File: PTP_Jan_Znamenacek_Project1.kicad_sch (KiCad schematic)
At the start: 0 parts

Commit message: Ispunjena sastavnica
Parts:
- added R1, R2: R_Small, symbol Device:R_Small
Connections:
- new net +3V3: R1.1
- new net GND: R2.2
- new net U_iz: R1.2, R2.1
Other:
- company: (none) -> TVZ
- title: (none) -> BCD Brojač

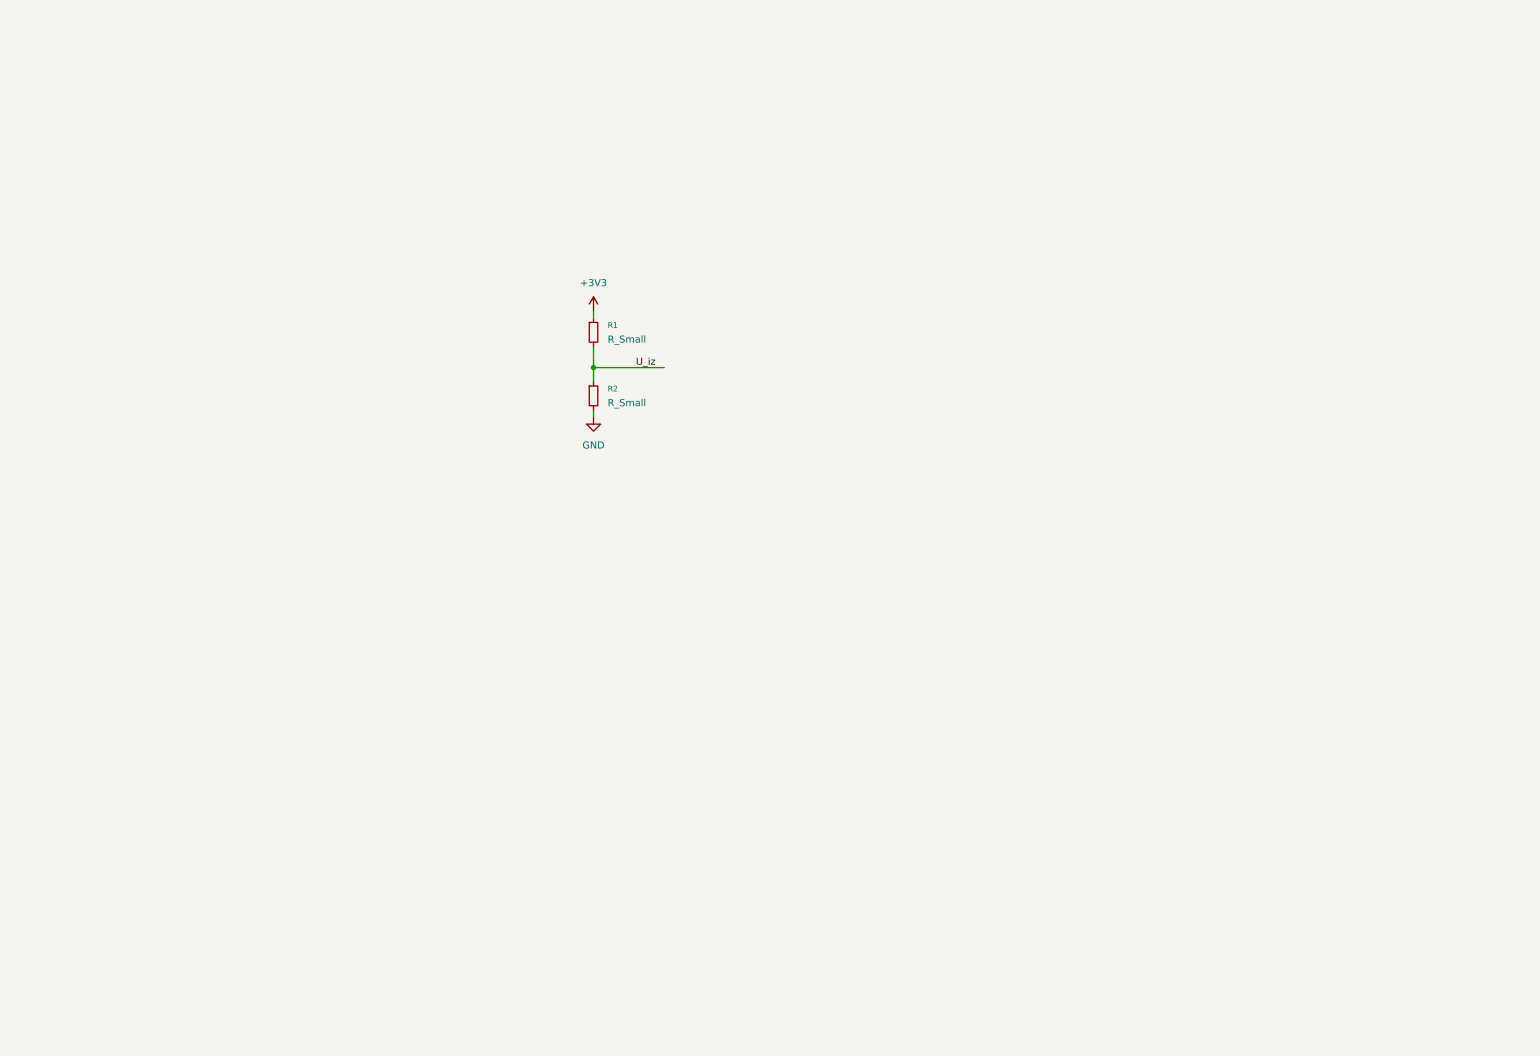
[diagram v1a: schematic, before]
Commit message: Dodan NE555P
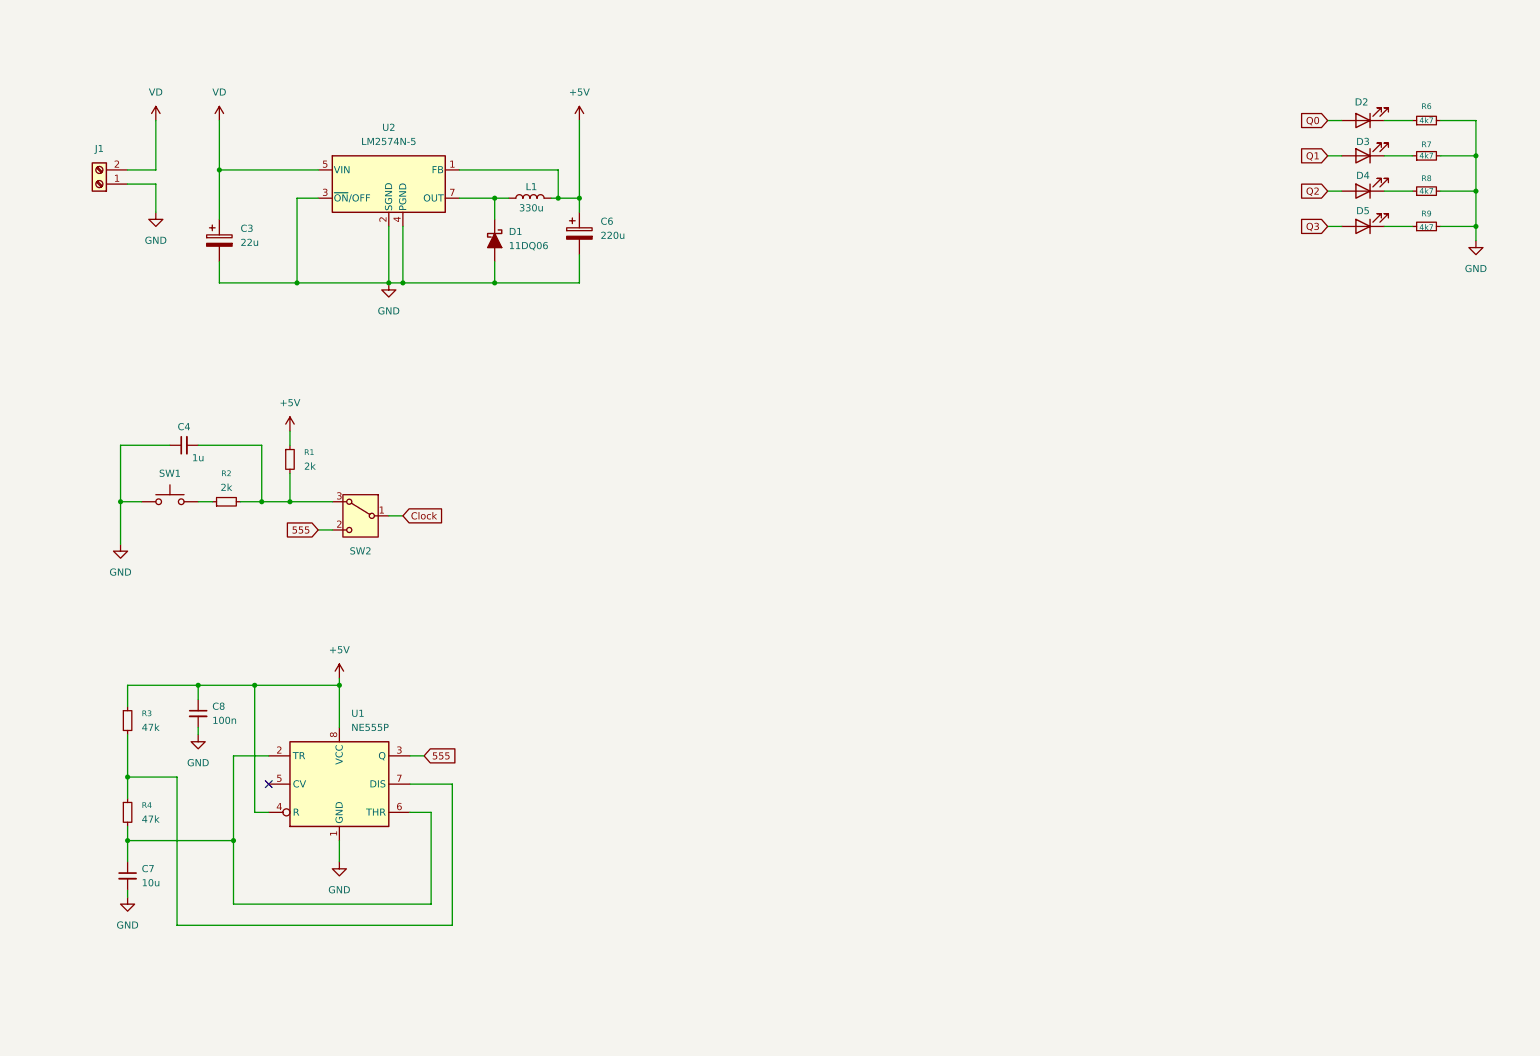
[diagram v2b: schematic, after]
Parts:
- added C3: 22u, symbol Device:C_Polarized
- added C4: 1u, symbol Device:C_Small
- added C6: 220u, symbol Device:C_Polarized
- added C7: 10u, symbol Device:C_Small
- added C8: 100n, symbol Device:C_Small
- added D1: 11DQ06, symbol Device:D_Schottky_Filled
- added D2, D3, D4, D5: LED, symbol Device:LED
- added J1: Screw_Terminal_01x02, symbol Connector:Screw_Terminal_01x02
- added L1: 330u, symbol Device:L
- added R3, R4: 47k, symbol Device:R_Small
- added R6, R7, R8, R9: 4k7, symbol Device:R_Small
- added SW1: ~, symbol Switch:SW_Push
- added SW2: ~, symbol Switch:SW_SPDT_312
- added U1: NE555P, Package_DIP:DIP-8_W7.62mm, symbol Timer:NE555P
- added U2: LM2574N-5, Package_DIP:DIP-8_W7.62mm, symbol Regulator_Switching:LM2574N-5
- R1, R2: value R_Small -> 2k
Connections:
- net GND: now also C3.2, C4.1, C6.2, C7.2, C8.2, D1.2 (A), J1.1 (Pin_1), R6.2, R7.2, R8.2, R9.2, SW1.1, U1.1 (GND), U2.2 (SGND), U2.3 (~{ON}/OFF), U2.4 (PGND); no longer R2.2
- net +3V3 renamed +5V
- net +5V: now also C6.1, C8.1, L1.2, R3.1, U1.4 (R), U1.8 (VCC), U2.1 (FB)
- net U_iz: no longer names the net of R1.2
- net U_iz: now also R2.2, C4.2, SW2.3 (A); no longer R2.1
- new net: D5.1 (K), R9.1
- new net: D1.1 (K), L1.1, U2.7 (OUT)
- new net: D4.1 (K), R8.1
- new net: D2.1 (K), R6.1
- new net: C7.1, R4.2, U1.2 (TR), U1.6 (THR)
- new net: D3.1 (K), R7.1
- new net: R2.1, SW1.2
- new net: R3.2, R4.1, U1.7 (DIS)
- new net 555: SW2.2 (C), U1.3 (Q)
- new net Clock: SW2.1 (B)
- new net Q0: D2.2 (A)
- new net Q1: D3.2 (A)
- new net Q2: D4.2 (A)
- new net Q3: D5.2 (A)
- new net VD: C3.1, J1.2 (Pin_2), U2.5 (VIN)
- no-connect marks 0 -> 1

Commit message: Footprint i simbol
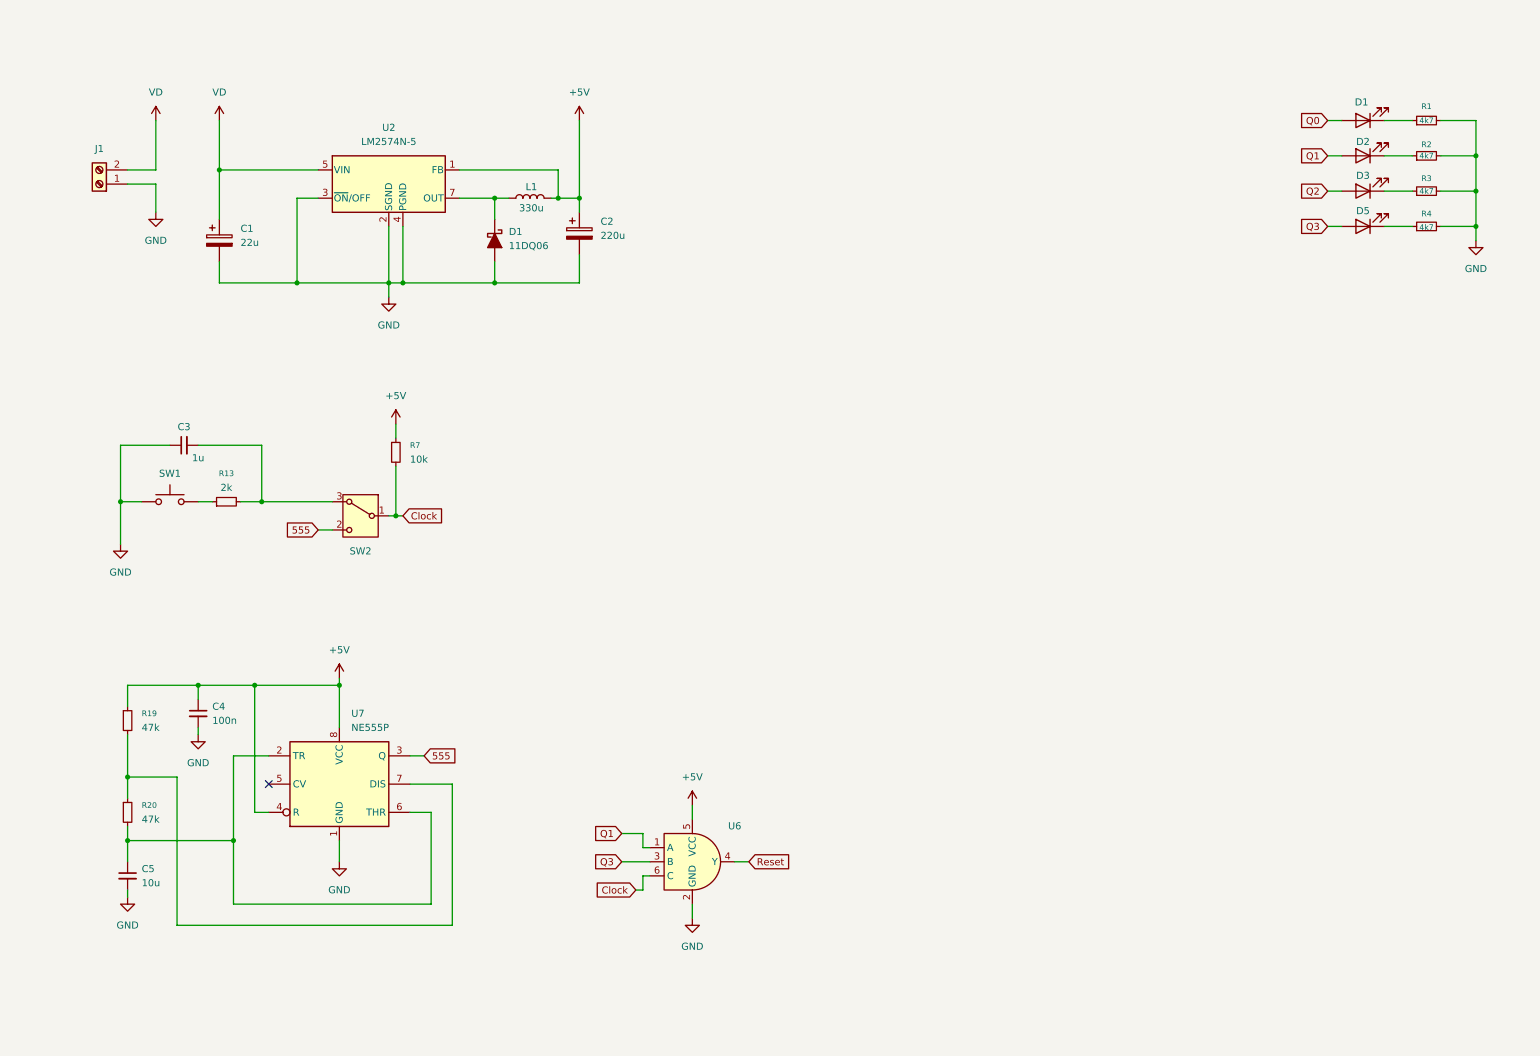
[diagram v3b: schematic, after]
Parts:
- added U6: ~, symbol SN74LVC1G11:SN74LVC1G11
- R7: renamed from R1; value 2k -> 10k
- renumbered C3 to C1, C6 to C2, C4 to C3, C8 to C4, C7 to C5, D2 to D1, D3 to D2, D4 to D3, R6 to R1, R2 to R13, R3 to R19, R7 to R2, R4 to R20, R8 to R3, R9 to R4, U1 to U7
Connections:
- net +5V: now also U6.5 (VCC)
- net Clock: now also R7.2, U6.6 (C)
- net GND: now also U6.2 (GND)
- net Q1: now also U6.1 (A)
- net Q3: now also U6.3 (B)
- net at C3.2, R13.2, SW2.3 (A): no longer R7.2
- new net Reset: U6.4 (Y)
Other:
- moved on the sheet: R7

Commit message: LV_4
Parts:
- added H1, H2, H3, H4: MountingHole, MountingHole:MountingHole_5.5mm, symbol Mechanical:MountingHole
- added R10, R11, R12, R15, R9: 10k, symbol Device:R_Small
- added R14, R16, R17, R18, R5, R6, R8: 2k, symbol Device:R_Small
- added U2: 74LS47, symbol 74xx:74LS47
- added U3, U4: 4027, symbol 4xxx:4027
- added U5: HDSP-7401, Display_7Segment:HDSP-7401, symbol Display_Character:HDSP-7401
- C1: footprint (none) -> Capacitor_THT:CP_Radial_D5.0mm_P2.00mm; Manufacturer (none) -> AISHI; Manufacturer Part Number (none) -> EWH1EM220D11OT
- C2: footprint (none) -> Capacitor_THT:CP_Radial_D5.0mm_P2.00mm; Manufacturer (none) -> SAMWHA; Manufacturer Part Number (none) -> RD1A227M05011BB
- C3: footprint (none) -> Capacitor_SMD:C_1206_3216Metric_Pad1.33x1.80mm_HandSolder; Manufacturer (none) -> SAMSUNG; Manufacturer Part Number (none) -> CL31B105KBHNNNE
- C4: footprint (none) -> Capacitor_SMD:C_1206_3216Metric_Pad1.33x1.80mm_HandSolder; Manufacturer (none) -> SAMSUNG; Manufacturer Part Number (none) -> CL31B104KBCNNNC
- C5: footprint (none) -> Capacitor_SMD:C_1206_3216Metric_Pad1.33x1.80mm_HandSolder; Manufacturer (none) -> SAMSUNG; Manufacturer Part Number (none) -> CL31A106KBHNNNE
- D1, D2, D3, D5: footprint (none) -> LED_THT:LED_D5.0mm
- D4: renamed from D1; footprint (none) -> Diode_THT:D_DO-41_SOD81_P12.70mm_Horizontal; Manufacturer (none) -> SMC DIODE SOLUTIONS; Manufacturer Part Number (none) -> 11DQ06TA
- J1: footprint (none) -> TerminalBlock_MetzConnect:TerminalBlock_MetzConnect_Type011_RT05502HBLC_1x02_P5.00mm_Horizontal; Manufacturer (none) -> DEGSON ELECTRONICS; Manufacturer Part Number (none) -> DG301-5.0-02P-12-00A(H)
- L1: footprint (none) -> Inductor_THT:L_Radial_D7.2mm_P3.00mm_Murata_1700; Manufacturer (none) -> FERROCORE; Manufacturer Part Number (none) -> COIL0608-0.33
- R1, R2, R3, R4: footprint (none) -> Resistor_THT:R_Axial_DIN0207_L6.3mm_D2.5mm_P10.16mm_Horizontal
- U6: value ~ -> 74LVC1G11
- renumbered U2 to U1
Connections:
- net +5V: now also R10.1, R11.1, R12.1, R15.2, R9.1, U2.16 (VCC), U3.16 (VDD), U4.16 (VDD), U5.1 (CA), U5.6 (CA)
- net Clock: now also U6.3 (B), U3.3 (C); no longer U6.6 (C)
- net GND: now also U2.8 (GND), U3.7 (S), U3.8 (VSS), U3.9 (S), U4.7 (S), U4.8 (VSS), U4.9 (S)
- net Q0: now also U2.7 (A), U3.1 (Q), U3.13 (C)
- net Q1: now also U6.6 (C), U2.1 (B), U3.15 (Q), U4.3 (C); no longer U6.1 (A)
- net Q2: now also U2.2 (C), U4.1 (Q), U4.13 (C)
- net Q3: now also U6.1 (A), U2.6 (D), U4.15 (Q); no longer U6.3 (B)
- net Reset: now also U3.12 (R), U3.4 (R), U4.12 (R), U4.4 (R)
- new net: R11.2, U4.5 (K), U4.6 (J)
- new net: R14.1, U2.10 (d)
- new net: R8.1, U2.11 (c)
- new net: R6.1, U2.12 (b)
- new net: R5.1, U2.13 (a)
- new net: R18.1, U2.14 (g)
- new net: R17.1, U2.15 (f)
- new net: R15.1, U2.3 (LT), U2.4 (BI), U2.5 (RBI)
- new net: R16.1, U2.9 (e)
- new net: R10.2, U3.10 (J), U3.11 (K)
- new net: R12.2, U4.10 (J), U4.11 (K)
- new net: R8.2, U5.8 (C)
- new net: R16.2, U5.4 (E)
- new net: R18.2, U5.3 (G)
- new net: R9.2, U3.5 (K), U3.6 (J)
- new net: R5.2, U5.10 (A)
- new net: R17.2, U5.2 (F)
- new net: R14.2, U5.5 (D)
- new net: R6.2, U5.9 (B)
- no-connect marks 1 -> 6
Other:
- note added: "555 Timer"
- note added: "JK Bistabili"
- note added: "LED Diode"
- note added: "Montažne rupe"
- note added: "Napajanje"
- note added: "Napajanje bistabila"
- note added: "Reset brojača"
- note added: "Tipkalo i ulaz radnog takta"
- moved on the sheet: C1, C2, C3, C4, C5, D1, D2, D3, D4, D5, J1, L1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

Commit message: PCB Pocetak
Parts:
- R10, R11, R12, R13, R14, R15, R16, R17, R18, R19, R20, R5, R6, R7, R8, R9: footprint (none) -> Resistor_SMD:R_1206_3216Metric_Pad1.30x1.75mm_HandSolder
- SW1: footprint (none) -> Button_Switch_THT:SW_PUSH_6mm_H4.3mm
- SW2: footprint (none) -> Button_Switch_THT:SW_Slide_SPDT_Straight_CK_OS102011MS2Q
- U2, U3, U4: footprint (none) -> Package_DIP:DIP-16_W7.62mm_Socket_LongPads
- U6: footprint (none) -> Package_TO_SOT_SMD:SOT-23-6
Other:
- moved on the sheet: C5, R19, U7
